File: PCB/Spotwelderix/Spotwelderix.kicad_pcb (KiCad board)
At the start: 2 copper layers, 100 x 70 mm, 65 parts, among them IC1 INA213AIDCKR, IC2 IXDD604SIA, IC3 IXDD604SIA, J1 OnOffTast, J2 probe+, J3 Conn_01x02_Male, J4 probe-, J6 Conn_01x02_Male, P1 CONN_01X09, Q1 IRFB7430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

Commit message: v4
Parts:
- removed F2, F3: 50A, my_parts:IMAXX_H1810-2x4
- removed IC3: IXDD604SIA, SamacSys_Parts:SOIC127P600X175-8N
- removed R12: 10k, Resistor_SMD:R_0805_2012Metric
- removed R14: 47k, Resistor_SMD:R_0805_2012Metric
- added C19: 10µ, Capacitor_SMD:C_1206_3216Metric, F.Cu at (119.3, 67.1)
- added U2: AD8209, Package_SO:MSOP-8_3x3mm_P0.65mm, F.Cu at (160.5, 83.8)
- added U3: AD8209, Package_SO:MSOP-8_3x3mm_P0.65mm, F.Cu at (119.5, 63.6)
- C15: value 10n -> 470p
- C16: value 100n -> 10µ; footprint Capacitor_SMD:C_0805_2012Metric_Pad1.18x1.45mm_HandSolder -> Capacitor_SMD:C_1206_3216Metric
- F1, F4: footprint my_parts:IMAXX_H1810-2x4 -> my_parts:Blade_Fuse_maxi_handsolder_1.5drill
- IC1: value INA213AIDCKR -> IXDD604SIA; footprint SamacSys_Parts:SOT65P210X110-6N -> mouser:SOIC127P600X175-8N
- IC2: footprint SamacSys_Parts:SOIC127P600X175-8N -> mouser:SOIC127P600X175-8N
- J3, J6: value Conn_01x02_Male -> XT90
- Q11: value BC817 -> DMG3402_SOT23_n_Fet_3A; footprint Package_TO_SOT_SMD:SOT-23 -> Package_TO_SOT_SMD:SOT-23_Handsoldering
- Q12: value BC807 -> DMG3402_SOT23_n_Fet_3A; footprint Package_TO_SOT_SMD:SOT-23 -> Package_TO_SOT_SMD:SOT-23_Handsoldering
- R10: value 470 -> 100
- R11, R13: value 47k -> 55k
- R4: value 10k -> 100
- R7: value 15k -> 133k
- R8: value 2.5k -> 100
- moved C17 39.5 mm to (150.9, 82.7)
- moved R13 36.1 mm to (150.9, 84.9)
- moved R10 35.9 mm to (154.9, 82.6), turned to 180 degrees
- moved IC2 34.8 mm to (174.4, 104.9), turned to 0 degrees
- moved Q12 32.7 mm to (145.8, 83.8), turned to 180 degrees
- moved IC1 28.0 mm to (139.8, 107.3), turned to 270 degrees
- moved Q11 22.8 mm to (108.4, 81.4), turned to 270 degrees
- moved P1 19.7 mm to (104.6, 63.3), turned to 270 degrees
- moved F1 17.3 mm to (165.7, 66.0), turned to 0 degrees
- moved C9 13.4 mm to (175.9, 80.7)
- moved F4 13.4 mm to (165.7, 76.0), turned to 0 degrees
- moved C7 12.2 mm to (169.6, 80.7)
- moved R4 12.0 mm to (113.6, 69.5), turned to 0 degrees
- moved C2 11.3 mm to (169.8, 86.2)
- moved C6 11.2 mm to (166.5, 80.7)
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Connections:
- C11 pad 2: GND -> Net-(C11-Pad2)
- C15 pad 1: V_Batt -> Net-(C15-Pad1)
- C16 pad 1: GND -> +5V
- C16 pad 2: +3V3 -> GND
- C17 pad 1: R_Schunt_Stab -> Net-(C17-Pad1)
- IC1 pad 1: GND -> VCC
- IC1 pad 2: GND -> Gate_logic
- IC1 pad 3: +3V3 -> GND
- IC1 pad 4: +BATT -> Gate_logic
- IC1 pad 5: VCCQ -> Gate
- IC1 pad 6: Net-(IC1-Pad6) -> VCC
- P1 pad 3: V_Batt -> Probe_diff
- P1 pad 6: +3V3 -> +5V
- Q11 pad 1: Net-(Q11-Pad1) -> EnablePower
- Q11 pad 3: Net-(Q11-Pad3) -> Net-(C11-Pad2)
- Q12 pad 1: Net-(Q12-Pad1) -> Gate_logic
- Q12 pad 2: Net-(Q12-Pad2) -> GND
- Q12 pad 3: VCCQ -> Net-(Q12-Pad3)
- R10 pad 1: Net-(Q11-Pad1) -> Net-(R10-Pad1)
- R10 pad 2: GND -> R_Schunt_Stab
- R11 pad 1: VCCQ -> Net-(C15-Pad1)
- R11 pad 2: Net-(Q12-Pad1) -> GND
- R13 pad 1: Net-(IC1-Pad6) -> Net-(C17-Pad1)
- R13 pad 2: R_Schunt_Stab -> Net-(Q12-Pad3)
- R4 pad 1: EnablePower -> Probe_diff
- R4 pad 2: Net-(Q11-Pad1) -> Net-(R4-Pad2)
- R7 pad 1: Net-(Q12-Pad2) -> Net-(R4-Pad2)
- R7 pad 2: Net-(R14-Pad1) -> Net-(C15-Pad1)
- R8 pad 1: Net-(R14-Pad1) -> Dallas
- R8 pad 2: GND -> Net-(R8-Pad2)
- R9 pad 2: GND -> Net-(C11-Pad2)
- U1 pad 2: Dallas -> Net-(R8-Pad2)
- U1 pad 3: +3V3 -> +5V
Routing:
- net +5V: track 0.00 -> 107.5 mm, vias 0 -> 1
- net Probe-: track 59.0 -> 157.6 mm, vias 48 -> 43
- net +3V3: track 90.8 -> 0.00 mm, vias 2 -> 0
- net Gate_logic: track 98.4 -> 167.6 mm, vias 6 -> 7
- net Net-(IC1-Pad6): track 67.2 -> 0.00 mm
- net R_Schunt_Stab: track 18.4 -> 69.1 mm, vias 0 -> 2
- net Net-(C11-Pad2): track 0.00 -> 45.7 mm
- net VCC: track 138.6 -> 110.2 mm
- net VCCQ: track 140.8 -> 165.5 mm, vias 0 -> 2
- net +BATT: track 5.86 -> 30.4 mm
- net GND: track 63.6 -> 45.2 mm, vias 92 -> 111
- net ProbeADC: track 67.0 -> 49.0 mm
- net V_Batt: track 17.1 -> 0.00 mm
- net EnablePower: track 29.9 -> 15.4 mm
- net Net-(R4-Pad2): track 0.00 -> 13.5 mm
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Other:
- board text added: "5V"
- board text added: "Probe_diff_U"
- board text added: "v03"
- board text removed: "3V3"
- board text removed: "V_Batt"
- board text removed: "v02"

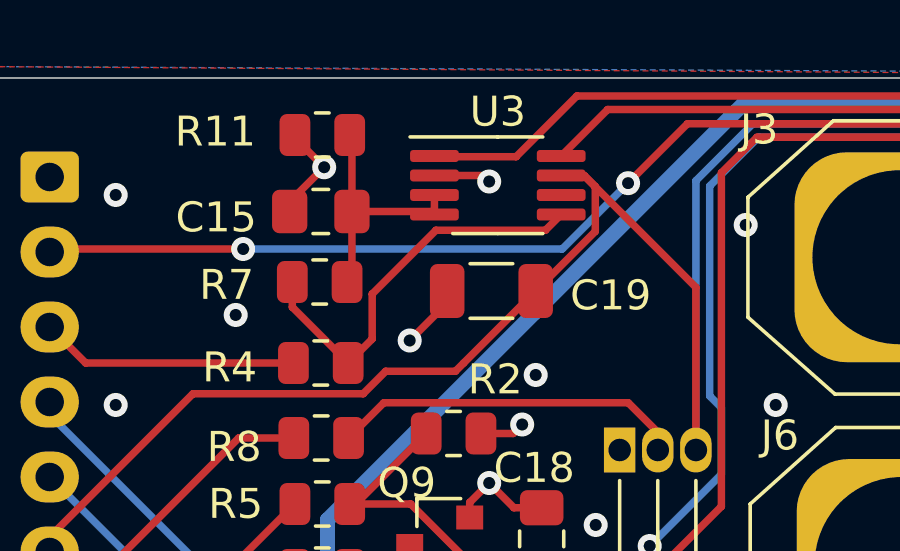
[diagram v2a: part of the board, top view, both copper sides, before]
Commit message: working display
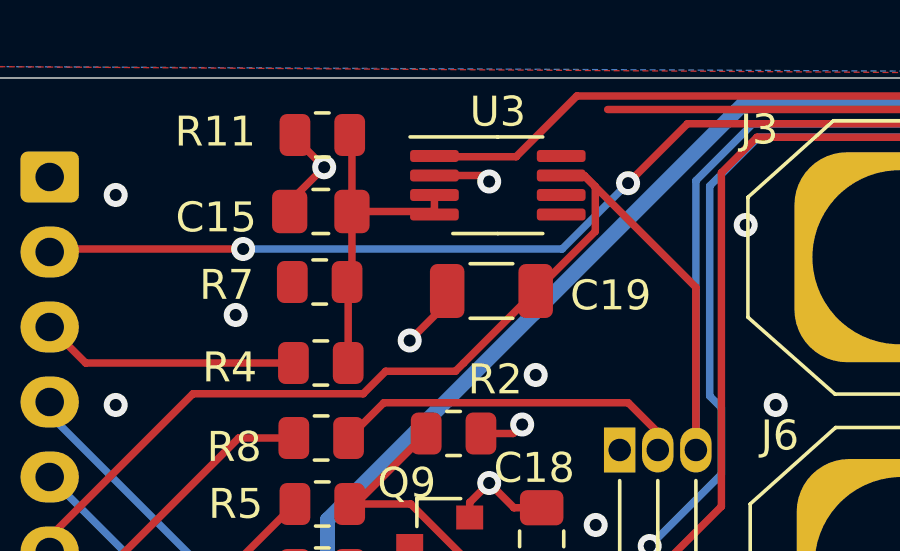
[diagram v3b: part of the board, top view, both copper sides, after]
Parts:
- R11: value 55k -> 2k5
- R7: value 133k -> 15k
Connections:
- R4 pad 2: Net-(R4-Pad2) -> Net-(C15-Pad1)
- R7 pad 1: Net-(R4-Pad2) -> VCCQ
- U3 pad 2: GND -> Net-(U3-Pad2)
- U3 pad 3: Net-(C15-Pad1) -> Net-(U3-Pad3)
- U3 pad 4: Net-(C15-Pad1) -> Net-(U3-Pad4)
- U3 pad 5: Net-(R4-Pad2) -> Net-(U3-Pad5)
- U3 pad 7: +5V -> Net-(U3-Pad7)
- U3 pad 8: VCCQ -> Net-(U3-Pad8)
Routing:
- net Net-(R4-Pad2): track 13.5 -> 0.00 mm
- net Net-(C15-Pad1): track 8.44 -> 11.2 mm
- net VCCQ: track 165.5 -> 163.3 mm
- net GND: track 45.2 -> 43.3 mm, vias 111 -> 110
- net Net-(U3-Pad2): track 0.00 -> 1.91 mm, vias 0 -> 1
